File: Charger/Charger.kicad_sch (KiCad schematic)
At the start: 69 parts, among them J1 Bat_ballanser_conn, Q1 BC846BW, Q10 MJD45H11T4, Q11 MJD45H11T4, Q12 MJD45H11T4, Q2 MJD45H11T4, Q3 BC846BW, Q4 MJD45H11T4, Q5 BC846BW, Q6 MJD45H11T4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

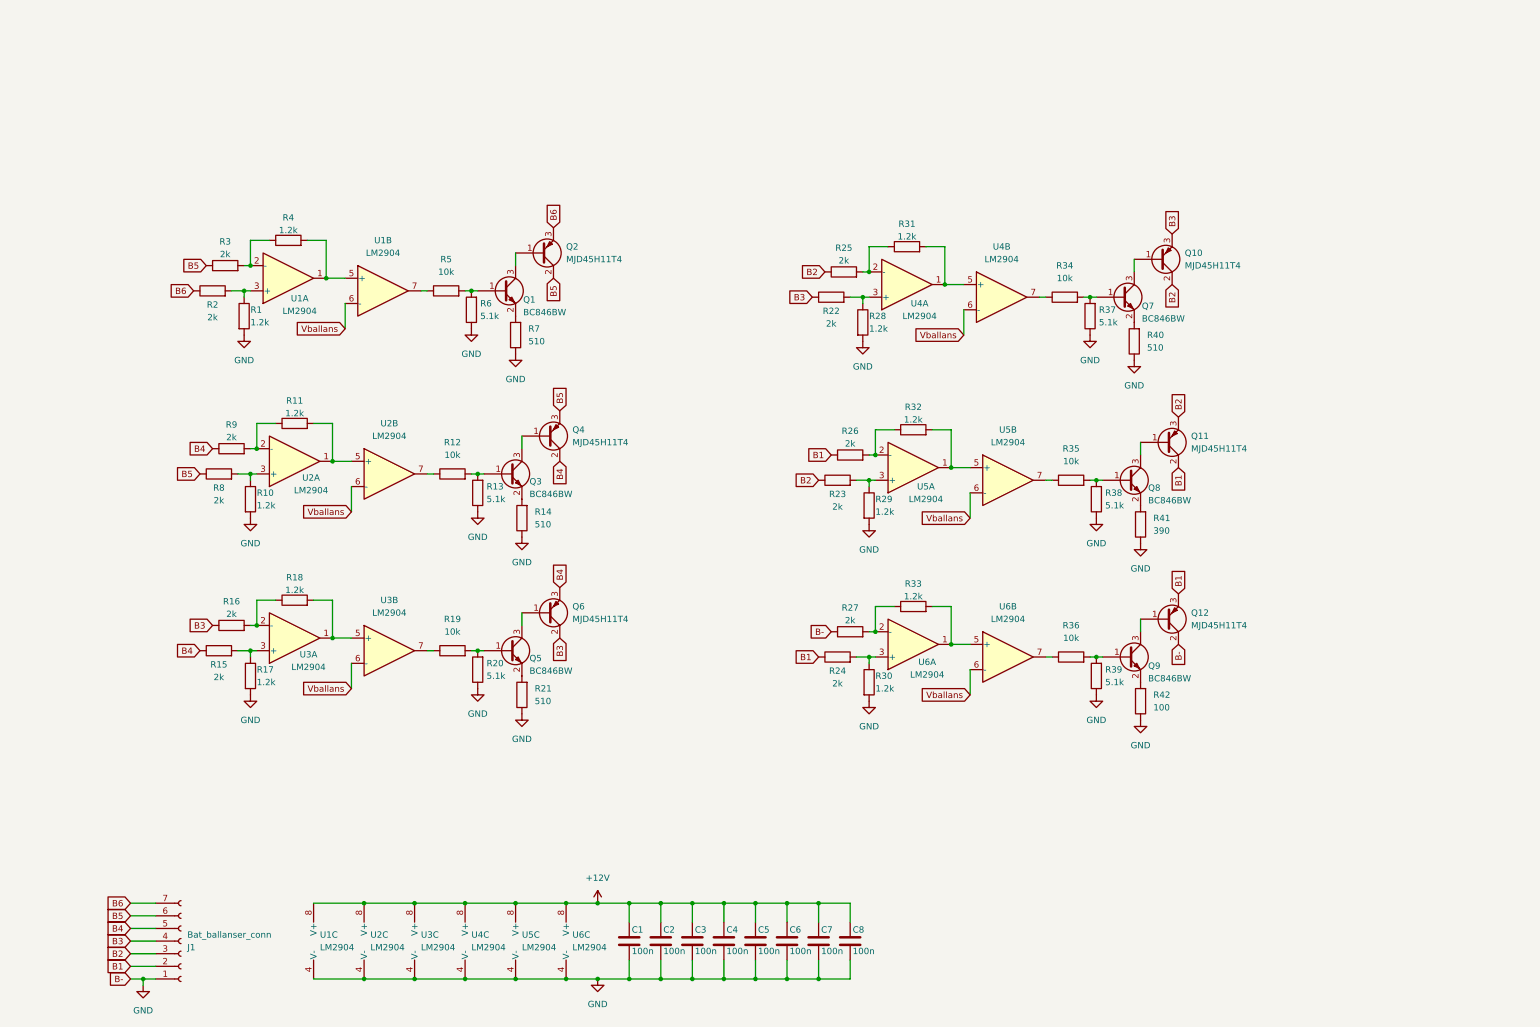
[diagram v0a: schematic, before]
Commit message: Update Charger.kicad_sch
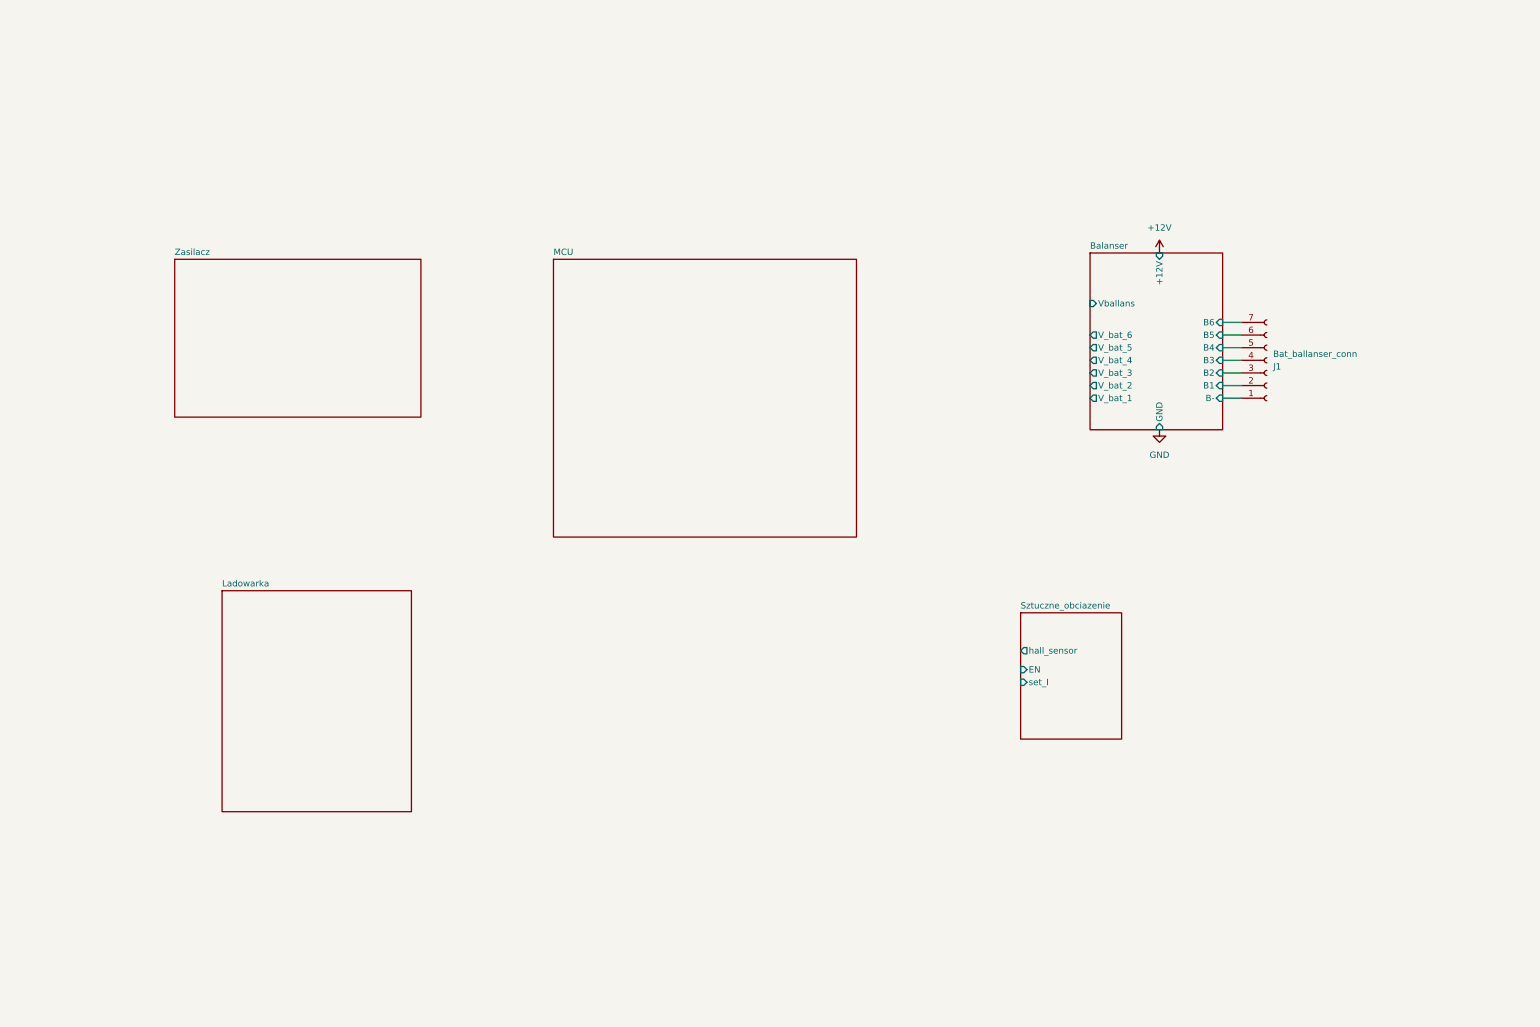
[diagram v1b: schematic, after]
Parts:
- removed C1, C2, C3, C4, C5, C6, C7, C8: 100n, Capacitor_SMD:C_0805_2012Metric_Pad1.18x1.45mm_HandSolder, symbol Device:C
- removed Q1, Q3, Q5, Q7, Q8, Q9: BC846BW, Package_TO_SOT_SMD:SOT-323_SC-70, symbol Transistor_BJT:BC846
- removed Q10, Q11, Q12, Q2, Q4, Q6: MJD45H11T4, Package_TO_SOT_SMD:TO-252-2, symbol Device:Q_PNP_BCE
- removed R1, R10, R11, R17, R18, R28, R29, R30, R31, R32, R33, R4: 1.2k, Resistor_SMD:R_0805_2012Metric_Pad1.20x1.40mm_HandSolder, symbol Device:R
- removed R12, R19, R34, R35, R36, R5: 10k, Resistor_SMD:R_0805_2012Metric_Pad1.20x1.40mm_HandSolder, symbol Device:R
- removed R13, R20, R37, R38, R39, R6: 5.1k, Resistor_SMD:R_0805_2012Metric_Pad1.20x1.40mm_HandSolder, symbol Device:R
- removed R14, R21, R40, R7: 510, Resistor_SMD:R_0805_2012Metric_Pad1.20x1.40mm_HandSolder, symbol Device:R
- removed R15, R16, R2, R22, R23, R24, R25, R26, R27, R3, R8, R9: 2k, Resistor_SMD:R_0805_2012Metric_Pad1.20x1.40mm_HandSolder, symbol Device:R
- removed R41: 390, Resistor_SMD:R_0805_2012Metric_Pad1.20x1.40mm_HandSolder, symbol Device:R
- removed R42: 100, Resistor_SMD:R_0805_2012Metric_Pad1.20x1.40mm_HandSolder, symbol Device:R
- removed U1, U2, U3, U4, U5, U6: LM2904, Package_SO:SO-8_3.9x4.9mm_P1.27mm, symbol Amplifier_Operational:LM2904
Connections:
- net GND: no longer J1.1 (Pin_1)
- net B1 renamed Balanser/B1
- net B2 renamed Balanser/B2
- net B3 renamed Balanser/B3
- net B4 renamed Balanser/B4
- net B5 renamed Balanser/B5
- net B6 renamed Balanser/B6
- new net Balanser/B-: J1.1 (Pin_1)
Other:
- added sheet Balanser (balanser.kicad_sch)
- added sheet Ladowarka (ladowarka.kicad_sch)
- added sheet MCU (mcu.kicad_sch)
- added sheet Sztuczne_obciazenie (sztuczne_obciazenie.kicad_sch)
- added sheet Zasilacz (zasilacz.kicad_sch)

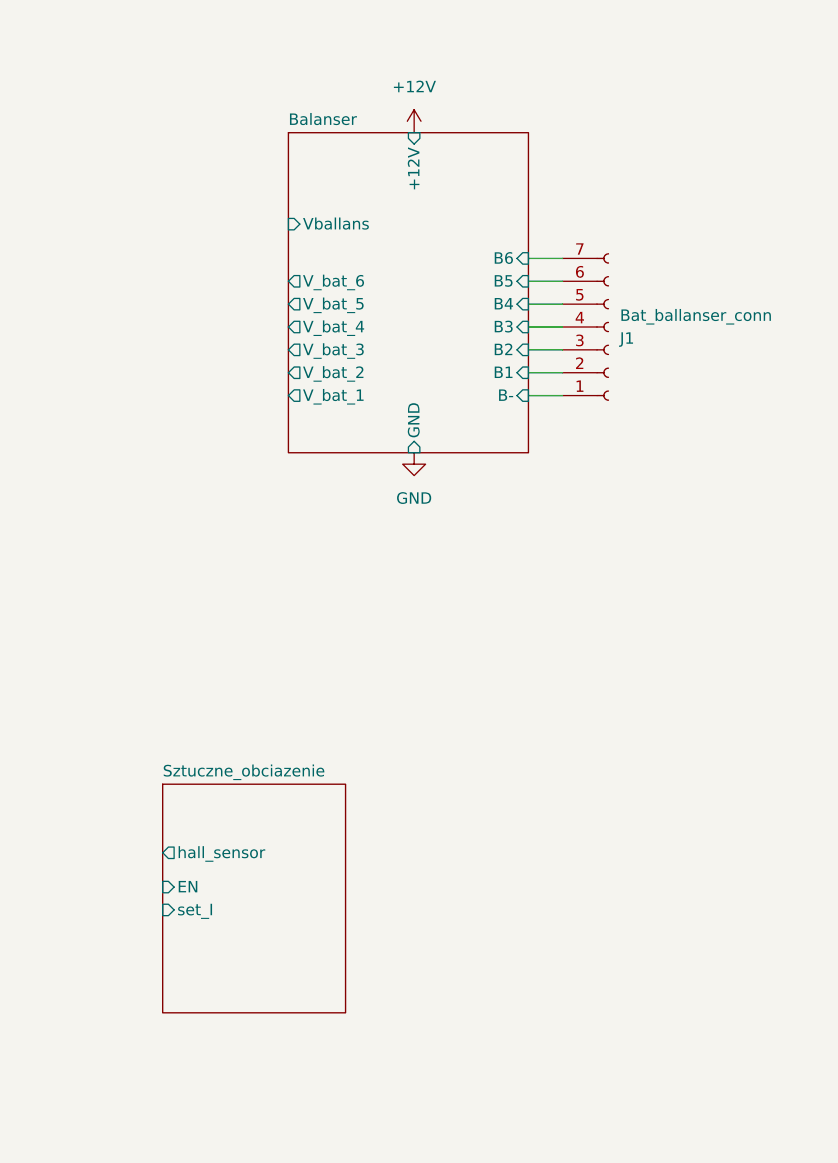
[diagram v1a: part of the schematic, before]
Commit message: powiar rw + zlacze baterii
koniecznie sprawdzić masy i flagi
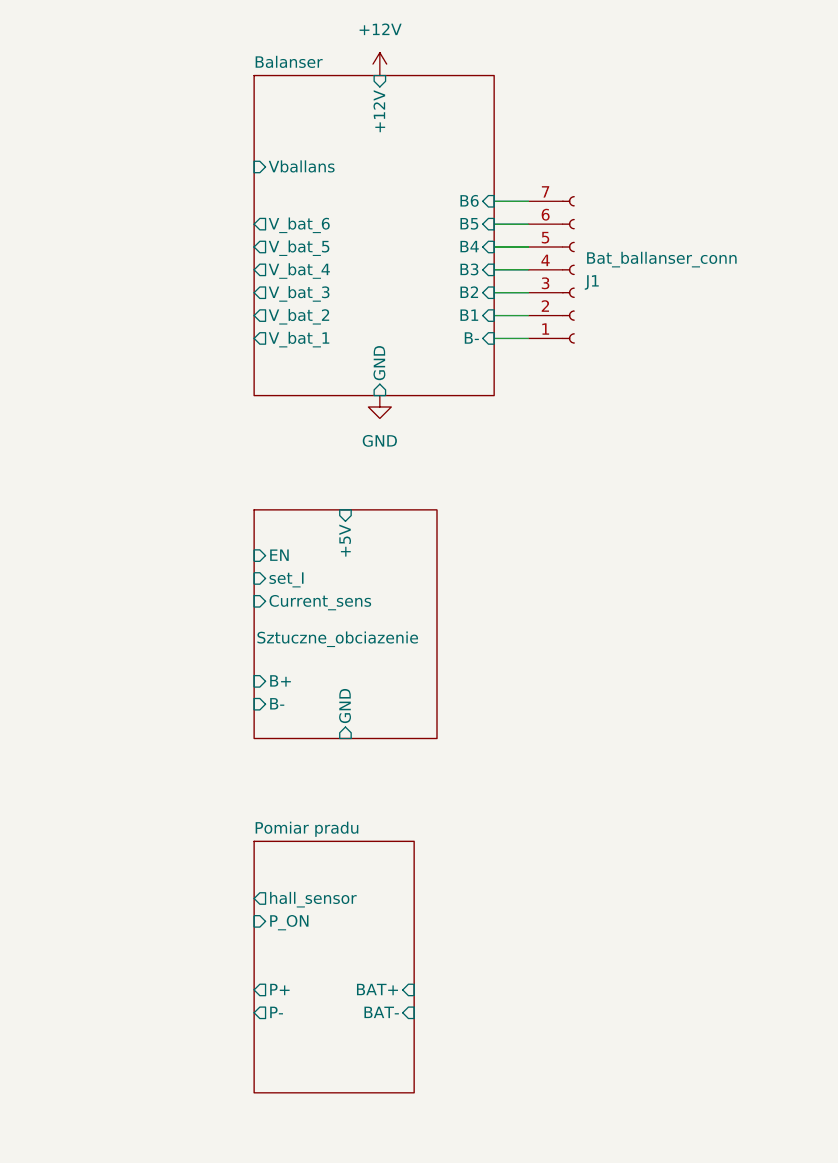
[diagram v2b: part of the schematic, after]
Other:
- added sheet Pomiar pradu (pomiar_pradu.kicad_sch)
- sheet Sztuczne_obciazenie ports: added +5V, B+, B-, Current_sens, GND; removed hall_sensor
- moved on the sheet: J1

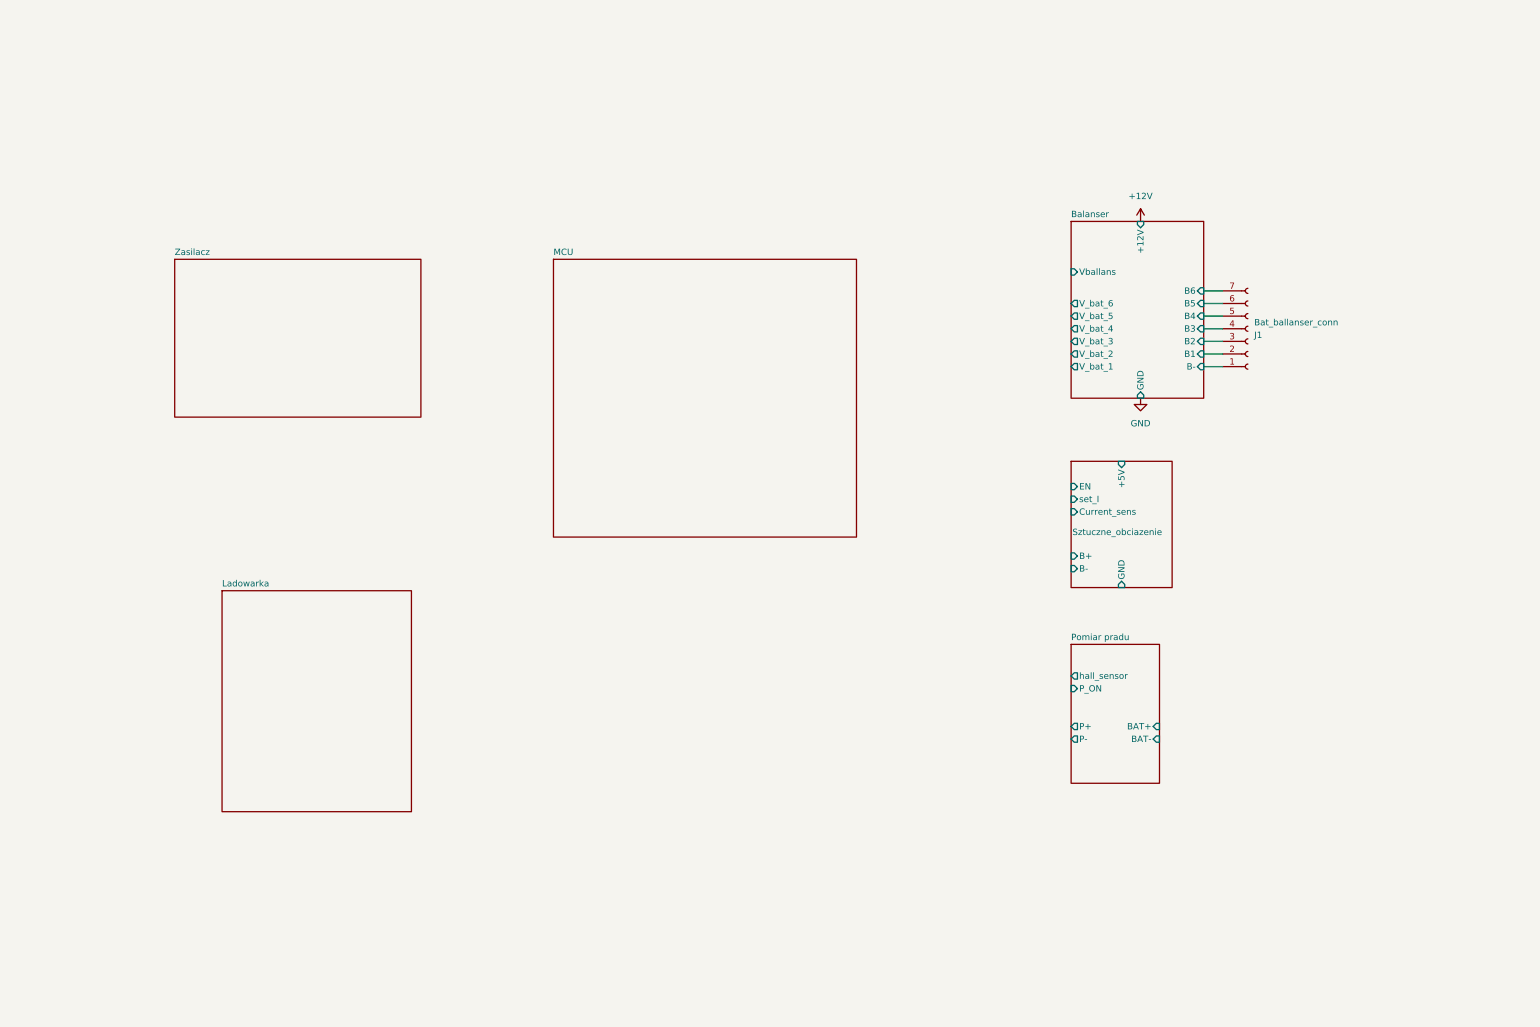
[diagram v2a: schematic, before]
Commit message: update
zakonczony schemat balansera, sztucznego obciazenia i pomiaru pradu. Przypisane wszystkie footprinty
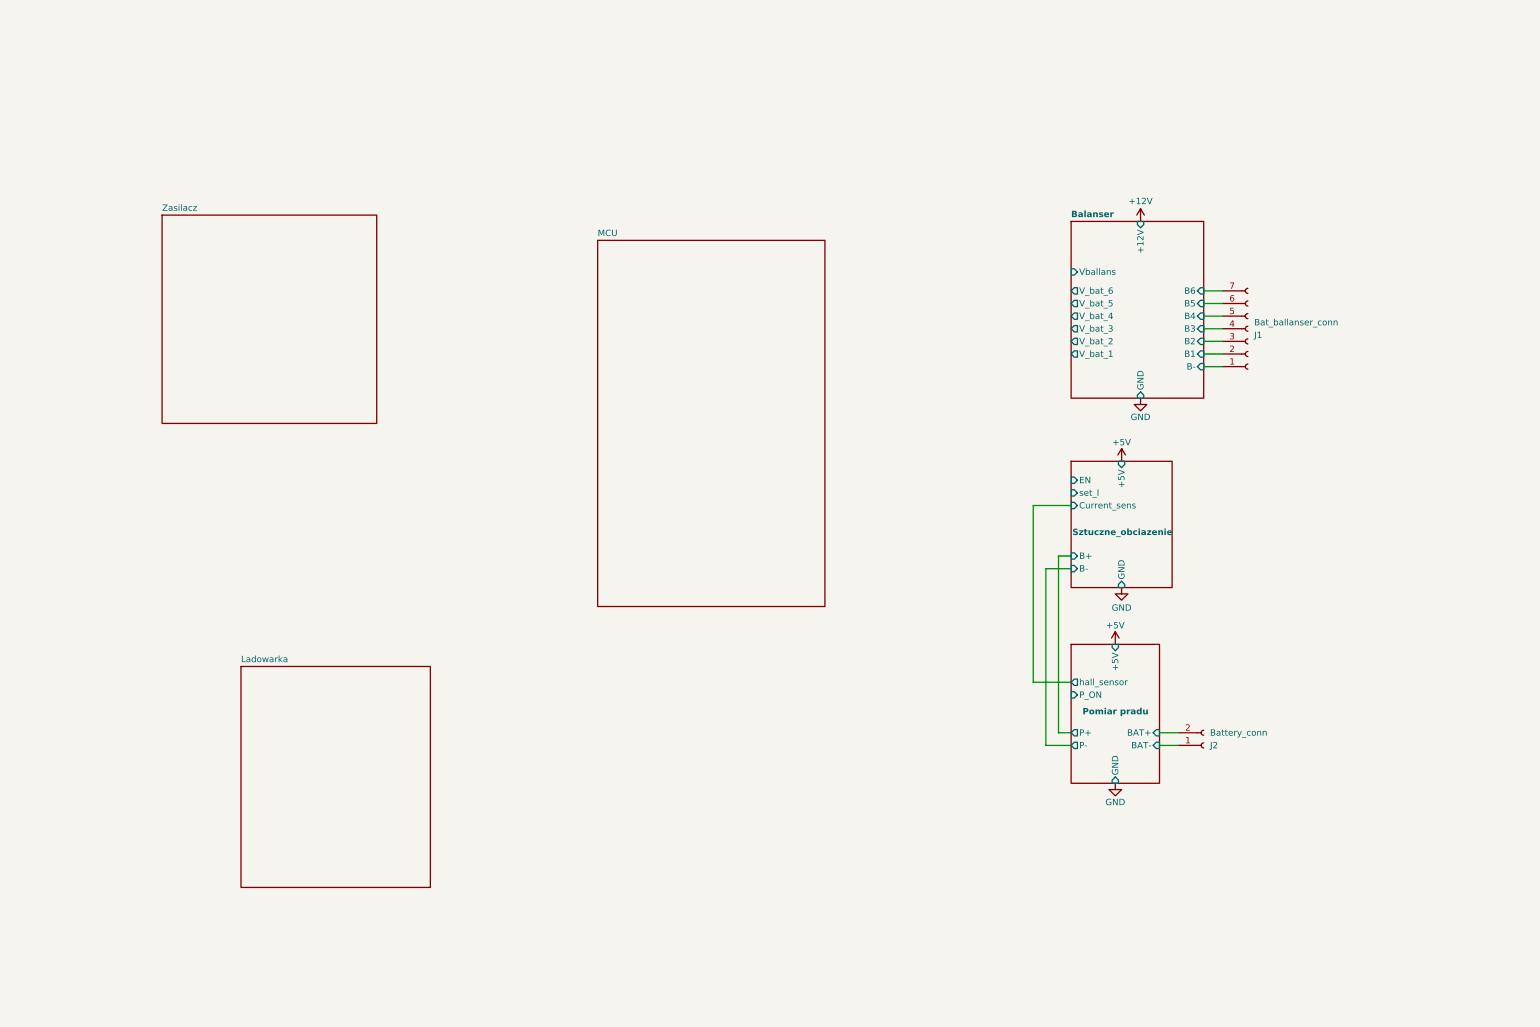
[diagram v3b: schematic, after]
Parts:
- added J2: Battery_conn, Connector_AMASS:AMASS_XT60PW-M_1x02_P7.20mm_Horizontal, symbol Connector:Conn_01x02_Socket
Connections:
- net Pomiar pradu/BAT+: now also J2.2 (Pin_2)
- net Pomiar pradu/BAT-: now also J2.1 (Pin_1)
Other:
- sheet Pomiar pradu ports: added +5V, GND; removed none

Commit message: obrocone zlacze balansera
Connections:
- net Balanser/B-: now also J1.7 (Pin_7); no longer J1.1 (Pin_1)
- net Balanser/B1: now also J1.6 (Pin_6); no longer J1.2 (Pin_2)
- net Balanser/B2: now also J1.5 (Pin_5); no longer J1.3 (Pin_3)
- net Balanser/B4: now also J1.3 (Pin_3); no longer J1.5 (Pin_5)
- net Balanser/B5: now also J1.2 (Pin_2); no longer J1.6 (Pin_6)
- net Balanser/B6: now also J1.1 (Pin_1); no longer J1.7 (Pin_7)
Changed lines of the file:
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@@
 		(lib_id "Connector:Conn_01x07_Socket")
 		(at 250.19 50.8 0)
-		(mirror x)
 		(unit 1)
 		(exclude_from_sim no)
@@
 		(on_board yes)
 		(dnp no)
-		(fields_autoplaced yes)
 		(property "Reference" "J1"
-			(at 251.46 52.0701 0)
+			(at 251.46 49.5299 0)
 			(effects
 				(font
@@
 		)
 		(property "Value" "Bat_ballanser_conn"
-			(at 251.46 49.5301 0)
+			(at 251.46 52.0699 0)
 			(effects
 				(font

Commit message: Opisy pinow modulow
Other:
- note added: "EN - podanie 3.3v załącza moduł set_I - podanie 5V ustawia 5A - moge przeskalować na 3.3 działa liniowo"
- note added: "P_ON - Podanie 3.3 V załącza baterie hall_sensor - 0A -> 1.65v +-1A -> +-0.066mV"
- note added: "Vball - napiecie balansowana podanie 3.3V ustawia balansowanie na 5V V_bat_x - napiecie na poszczególnym ogniwie 5V na ogniwie odpowiada 3.3V na pinie"
- note added: "do sprawdzenia na bardzo poważnie czy hall jest dobrze włożony do schematu tzn jesli pchamy prąd do baterii to napiecie bedzie ponizej 1.65 a jesli pobieramy z baterii to czy bedzie rosło"
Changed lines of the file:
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@@
+		)
+	)
+	(text "EN - podanie 3.3v załącza moduł\nset_I - podanie 5V ustawia 5A - moge przeskalować na 3.3 działa liniowo"
+		(exclude_from_sim no)
+		(at 203.708 70.358 0)
+		(effects
+			(font
+				(size 1.27 1.27)
+			)
+		)
+	)
+	(text "Vball - napiecie balansowana podanie 3.3V ustawia balansowanie na 5V \nV_bat_x - napiecie na poszczególnym ogniwie 5V na ogniwie odpowiada 3.3V na pinie \n"
+		(exclude_from_sim no)
+		(at 231.394 21.082 0)
+		(effects
+			(font
+				(size 1.27 1.27)
+			)
+		)
+	)
+	(text "do sprawdzenia na bardzo poważnie czy hall jest dobrze włożony do schematu\n tzn jesli pchamy prąd do baterii to napiecie bedzie ponizej 1.65 a jesli \npobieramy z baterii to czy bedzie rosło"
+		(exclude_from_sim no)
+		(at 94.488 181.864 0)
+		(effects
+			(font
+				(size 2.54 2.54)
+			)
+		)
+	)
+	(text "P_ON - Podanie 3.3 V załącza baterie\nhall_sensor - 0A -> 1.65v  +-1A -> +-0.066mV"
+		(exclude_from_sim no)
+		(at 218.44 150.114 0)
+		(effects
+			(font
+				(size 1.27 1.27)
+			)
 		)
 	)
